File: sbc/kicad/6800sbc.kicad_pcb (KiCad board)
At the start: 2 copper layers, 104 parts, among them J1 AC/DC IN, J10 BAUD RATE, J11 SEGMENT TEST, J2 5V IN, J3 EXPANSION, J4 LTC, J5 Parallel Port, J6 TX DATA SELECT, J7 RX DATA SELECT, J8 USB POWER, J9 FTDI SERIAL, SW10 "9", SW11 "4", SW12 "5", SW13 "6", SW14 "1", SW15 "2", SW16 "3", SW17 "0", SW18 "RESET", SW2 "D", SW3 "E", SW4 "F", SW5 "A", SW6 "B", SW7 "C", SW8 "7", SW9 "8", U1 LM7805, U10 MAN71A, U11 MAN71A, U12 74LS259, U13 74LS259, U14 74LS259, U15 74LS259, U16 74LS259, U17 74LS259, U18 74LS244, U19 62256 RAM, U2 74LS00, U20 27128, U21 MC6802, U22 ATF16V8B, U23 74LS244, U24 74LS42, U3 74LS04, U4 6821, U5 MC6850, U6 MAN71A, U7 MAN71A, U8 MAN71A, U9 MAN71A, Y1 1.8432 MHz, Y2 3.579545 kHz

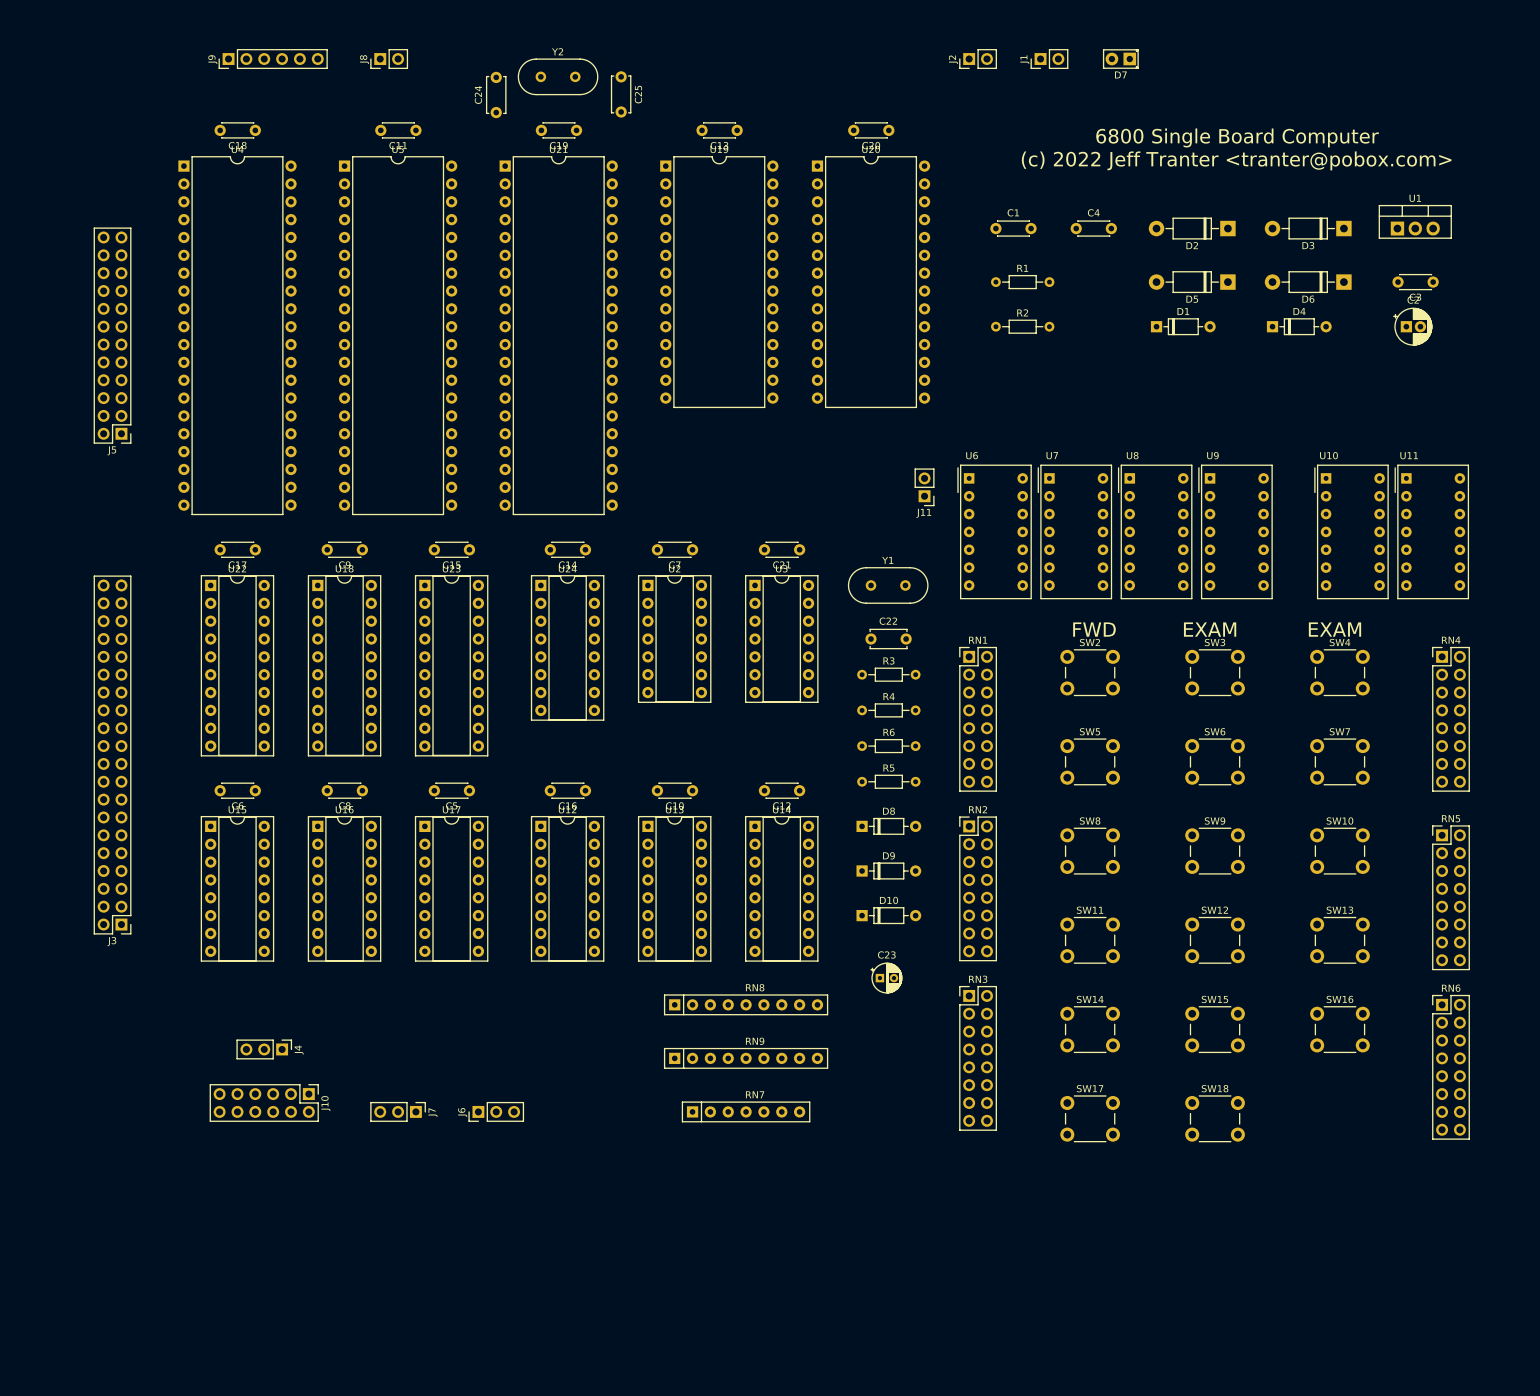
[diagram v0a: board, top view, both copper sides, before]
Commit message: Some fixes based on prototyping work.
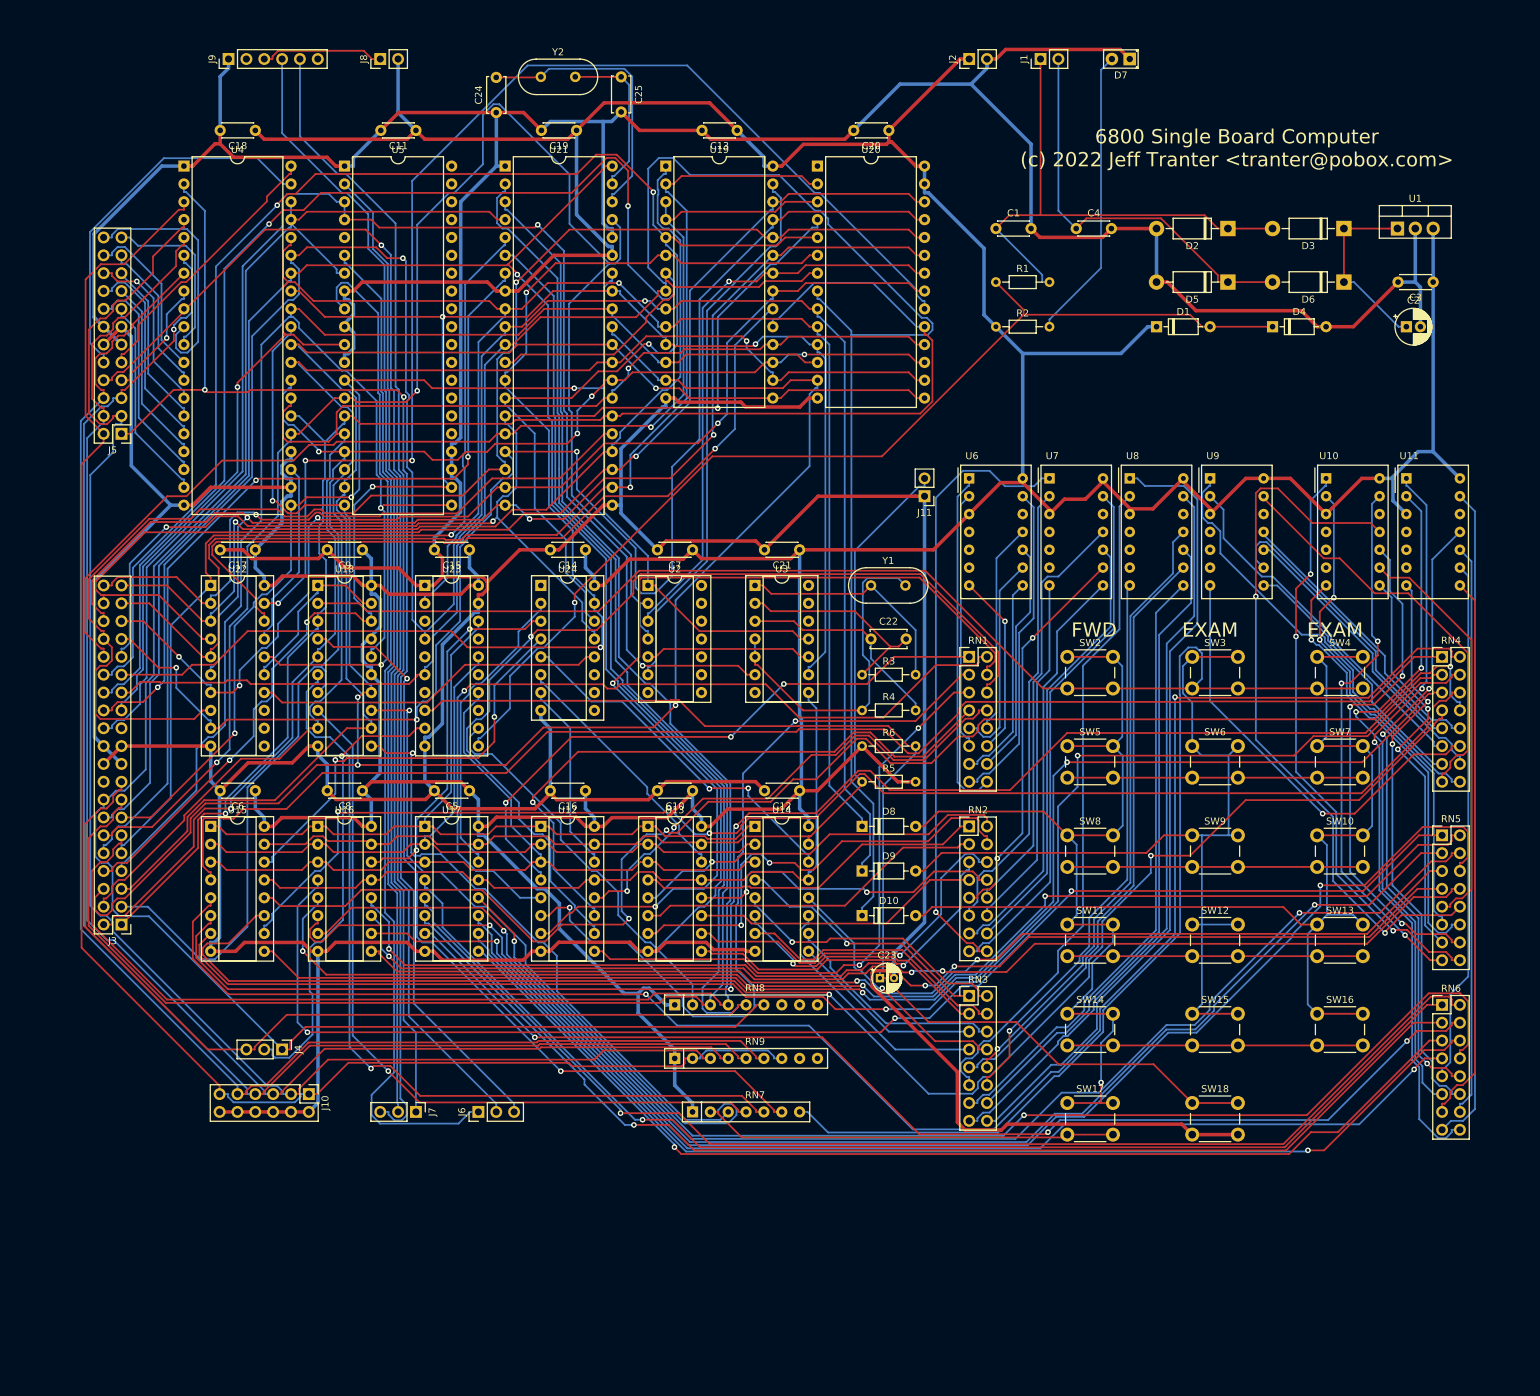
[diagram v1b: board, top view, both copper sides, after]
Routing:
- net GND: track 0.00 -> 998.2 mm
- net VCC: track 0.00 -> 904.0 mm
- net A1: track 0.00 -> 332.5 mm, vias 0 -> 3
- net ~RESET: track 0.00 -> 311.4 mm, vias 0 -> 1
- net A2: track 0.00 -> 298.9 mm
- net A0: track 0.00 -> 291.0 mm, vias 0 -> 2
- net Net-(RN7-Pad7): track 0.00 -> 276.5 mm
- net D2: track 0.00 -> 267.2 mm, vias 0 -> 4
- net ~IRQ: track 0.00 -> 262.0 mm
- net ~NMI: track 0.00 -> 256.9 mm
- net Net-(RN4-Pad2): track 0.00 -> 251.2 mm, vias 0 -> 2
- net D0: track 0.00 -> 249.0 mm, vias 0 -> 5
- net A5: track 0.00 -> 248.8 mm, vias 0 -> 3
- net ~HALT: track 0.00 -> 247.1 mm
- net MR: track 0.00 -> 239.9 mm
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
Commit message: Various updates.
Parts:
- removed RN1, RN2, RN3, RN4, RN5, RN6: 470, Connector_PinHeader_2.54mm:PinHeader_2x08_P2.54mm_Vertical
- added J12: REG. POWER, Connector_PinHeader_2.54mm:PinHeader_1x02_P2.54mm_Vertical, F.Cu at (199.4, 29.2)
- added R10: 470, Resistor_THT:R_Axial_DIN0204_L3.6mm_D1.6mm_P7.62mm_Horizontal, F.Cu at (168.9, 74.9)
- added R11: 470, Resistor_THT:R_Axial_DIN0204_L3.6mm_D1.6mm_P7.62mm_Horizontal, F.Cu at (168.9, 72.4)
- added R12: 470, Resistor_THT:R_Axial_DIN0204_L3.6mm_D1.6mm_P7.62mm_Horizontal, F.Cu at (168.9, 69.8)
- added R13: 470, Resistor_THT:R_Axial_DIN0204_L3.6mm_D1.6mm_P7.62mm_Horizontal, F.Cu at (168.9, 67.3)
- added R14: 470, Resistor_THT:R_Axial_DIN0204_L3.6mm_D1.6mm_P7.62mm_Horizontal, F.Cu at (168.9, 64.8)
- added R15: 470, Resistor_THT:R_Axial_DIN0204_L3.6mm_D1.6mm_P7.62mm_Horizontal, F.Cu at (180.3, 82.5)
- added R16: 470, Resistor_THT:R_Axial_DIN0204_L3.6mm_D1.6mm_P7.62mm_Horizontal, F.Cu at (180.3, 80.0)
- added R17: 470, Resistor_THT:R_Axial_DIN0204_L3.6mm_D1.6mm_P7.62mm_Horizontal, F.Cu at (180.3, 77.5)
- added R18: 470, Resistor_THT:R_Axial_DIN0204_L3.6mm_D1.6mm_P7.62mm_Horizontal, F.Cu at (180.3, 74.9)
- added R19: 470, Resistor_THT:R_Axial_DIN0204_L3.6mm_D1.6mm_P7.62mm_Horizontal, F.Cu at (180.3, 72.4)
- added R20: 470, Resistor_THT:R_Axial_DIN0204_L3.6mm_D1.6mm_P7.62mm_Horizontal, F.Cu at (180.3, 69.8)
- added R21: 470, Resistor_THT:R_Axial_DIN0204_L3.6mm_D1.6mm_P7.62mm_Horizontal, F.Cu at (180.3, 67.3)
- added R22: 470, Resistor_THT:R_Axial_DIN0204_L3.6mm_D1.6mm_P7.62mm_Horizontal, F.Cu at (180.3, 64.8)
- added R23: 470, Resistor_THT:R_Axial_DIN0204_L3.6mm_D1.6mm_P7.62mm_Horizontal, F.Cu at (191.8, 82.5)
- added R24: 470, Resistor_THT:R_Axial_DIN0204_L3.6mm_D1.6mm_P7.62mm_Horizontal, F.Cu at (191.8, 80.0)
- added R25: 470, Resistor_THT:R_Axial_DIN0204_L3.6mm_D1.6mm_P7.62mm_Horizontal, F.Cu at (191.8, 77.5)
- added R26: 470, Resistor_THT:R_Axial_DIN0204_L3.6mm_D1.6mm_P7.62mm_Horizontal, F.Cu at (191.8, 74.9)
- added R27: 470, Resistor_THT:R_Axial_DIN0204_L3.6mm_D1.6mm_P7.62mm_Horizontal, F.Cu at (191.8, 72.4)
- added R28: 470, Resistor_THT:R_Axial_DIN0204_L3.6mm_D1.6mm_P7.62mm_Horizontal, F.Cu at (191.8, 69.8)
- added R29: 470, Resistor_THT:R_Axial_DIN0204_L3.6mm_D1.6mm_P7.62mm_Horizontal, F.Cu at (191.8, 67.3)
- added R30: 470, Resistor_THT:R_Axial_DIN0204_L3.6mm_D1.6mm_P7.62mm_Horizontal, F.Cu at (191.8, 64.8)
- added R31: 470, Resistor_THT:R_Axial_DIN0204_L3.6mm_D1.6mm_P7.62mm_Horizontal, F.Cu at (203.2, 82.5)
- added R32: 470, Resistor_THT:R_Axial_DIN0204_L3.6mm_D1.6mm_P7.62mm_Horizontal, F.Cu at (203.2, 80.0)
- added R33: 470, Resistor_THT:R_Axial_DIN0204_L3.6mm_D1.6mm_P7.62mm_Horizontal, F.Cu at (203.2, 77.5)
- added R34: 470, Resistor_THT:R_Axial_DIN0204_L3.6mm_D1.6mm_P7.62mm_Horizontal, F.Cu at (203.2, 74.9)
- added R35: 470, Resistor_THT:R_Axial_DIN0204_L3.6mm_D1.6mm_P7.62mm_Horizontal, F.Cu at (203.2, 72.4)
- added R36: 470, Resistor_THT:R_Axial_DIN0204_L3.6mm_D1.6mm_P7.62mm_Horizontal, F.Cu at (203.2, 69.8)
- added R37: 470, Resistor_THT:R_Axial_DIN0204_L3.6mm_D1.6mm_P7.62mm_Horizontal, F.Cu at (203.2, 67.3)
- added R38: 470, Resistor_THT:R_Axial_DIN0204_L3.6mm_D1.6mm_P7.62mm_Horizontal, F.Cu at (203.2, 64.8)
- added R39: 470, Resistor_THT:R_Axial_DIN0204_L3.6mm_D1.6mm_P7.62mm_Horizontal, F.Cu at (219.7, 82.5)
- added R40: 470, Resistor_THT:R_Axial_DIN0204_L3.6mm_D1.6mm_P7.62mm_Horizontal, F.Cu at (219.7, 80.0)
- added R41: 470, Resistor_THT:R_Axial_DIN0204_L3.6mm_D1.6mm_P7.62mm_Horizontal, F.Cu at (219.7, 77.5)
- added R42: 470, Resistor_THT:R_Axial_DIN0204_L3.6mm_D1.6mm_P7.62mm_Horizontal, F.Cu at (219.7, 74.9)
- added R43: 470, Resistor_THT:R_Axial_DIN0204_L3.6mm_D1.6mm_P7.62mm_Horizontal, F.Cu at (219.7, 72.4)
- added R44: 470, Resistor_THT:R_Axial_DIN0204_L3.6mm_D1.6mm_P7.62mm_Horizontal, F.Cu at (219.7, 69.8)
- added R45: 470, Resistor_THT:R_Axial_DIN0204_L3.6mm_D1.6mm_P7.62mm_Horizontal, F.Cu at (219.7, 67.3)
- added R46: 470, Resistor_THT:R_Axial_DIN0204_L3.6mm_D1.6mm_P7.62mm_Horizontal, F.Cu at (219.7, 64.8)
- added R47: 470, Resistor_THT:R_Axial_DIN0204_L3.6mm_D1.6mm_P7.62mm_Horizontal, F.Cu at (231.1, 82.5)
- added R48: 470, Resistor_THT:R_Axial_DIN0204_L3.6mm_D1.6mm_P7.62mm_Horizontal, F.Cu at (231.1, 80.0)
- added R49: 470, Resistor_THT:R_Axial_DIN0204_L3.6mm_D1.6mm_P7.62mm_Horizontal, F.Cu at (231.1, 77.5)
- added R50: 470, Resistor_THT:R_Axial_DIN0204_L3.6mm_D1.6mm_P7.62mm_Horizontal, F.Cu at (231.1, 74.9)
- added R51: 470, Resistor_THT:R_Axial_DIN0204_L3.6mm_D1.6mm_P7.62mm_Horizontal, F.Cu at (231.1, 72.4)
- added R52: 470, Resistor_THT:R_Axial_DIN0204_L3.6mm_D1.6mm_P7.62mm_Horizontal, F.Cu at (231.1, 69.8)
- added R53: 470, Resistor_THT:R_Axial_DIN0204_L3.6mm_D1.6mm_P7.62mm_Horizontal, F.Cu at (231.1, 67.3)
- added R54: 470, Resistor_THT:R_Axial_DIN0204_L3.6mm_D1.6mm_P7.62mm_Horizontal, F.Cu at (231.1, 64.8)
- added R7: 470, Resistor_THT:R_Axial_DIN0204_L3.6mm_D1.6mm_P7.62mm_Horizontal, F.Cu at (168.9, 82.5)
- added R8: 470, Resistor_THT:R_Axial_DIN0204_L3.6mm_D1.6mm_P7.62mm_Horizontal, F.Cu at (168.9, 80.0)
- added R9: 470, Resistor_THT:R_Axial_DIN0204_L3.6mm_D1.6mm_P7.62mm_Horizontal, F.Cu at (168.9, 77.5)
- moved C1 14.0 mm to (172.7, 39.4)
- moved C4 14.0 mm to (184.2, 39.4)
- moved D2 14.0 mm to (205.7, 39.4)
- moved D3 14.0 mm to (222.2, 39.4)
- moved U1 14.0 mm to (229.9, 39.4)
- moved C2 14.0 mm to (231.1, 53.3)
- moved C3 14.0 mm to (234.9, 47.0)
- moved D1 14.0 mm to (195.6, 53.3)
- moved D4 14.0 mm to (212.1, 53.3)
- moved D5 14.0 mm to (205.7, 47.0)
- moved D6 14.0 mm to (222.2, 47.0)
- moved R1 14.0 mm to (172.7, 47.0)
- moved R2 14.0 mm to (172.7, 53.3)
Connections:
- C3 pad 1: VCC -> Net-(C3-Pad1)
- J10 pad 11: PA1 -> PA6
- RN9 pad 7: PA1 -> PA6
- U1 pad 3: VCC -> Net-(C3-Pad1)
- U19 pad 4: A7 -> A6
- U2 pad 10: (no net) -> GND
- U2 pad 12: (no net) -> GND
- U2 pad 13: (no net) -> GND
- U2 pad 9: (no net) -> GND
- U20 pad 1: (no net) -> VCC
- U3 pad 13: (no net) -> GND
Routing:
- net VCC: track 904.0 -> 896.4 mm
- net Net-(C3-Pad1): track 0.00 -> 7.62 mm
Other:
- board text added: "AUTO"
- board text added: "BACK"
- board text added: "CHAN"
- board text added: "DO"

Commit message: Getting close to ready to order PCBs. Check in all files.
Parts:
- removed RN7: 8K2, Resistor_THT:R_Array_SIP7
- removed RN8, RN9: 3K, Resistor_THT:R_Array_SIP9
- added H1: MountingHole_3mm, MountingHole:MountingHole_3mm, F.Cu at (39.4, 29.2)
- added H2: MountingHole_3mm, MountingHole:MountingHole_3mm, F.Cu at (215.9, 27.9)
- added H3: MountingHole_3mm, MountingHole:MountingHole_3mm, F.Cu at (38.1, 210.8)
- added H4: MountingHole_3mm, MountingHole:MountingHole_3mm, F.Cu at (215.9, 210.8)
- added J13: PA2, Connector_PinHeader_2.54mm:PinHeader_1x03_P2.54mm_Vertical, F.Cu at (74.9, 188.0)
- added J14: PA3, Connector_PinHeader_2.54mm:PinHeader_1x03_P2.54mm_Vertical, F.Cu at (78.7, 188.0)
- added J15: PA4, Connector_PinHeader_2.54mm:PinHeader_1x03_P2.54mm_Vertical, F.Cu at (82.5, 188.0)
- added J16: PA5, Connector_PinHeader_2.54mm:PinHeader_1x03_P2.54mm_Vertical, F.Cu at (86.4, 188.0)
- added J17: PA6, Connector_PinHeader_2.54mm:PinHeader_1x03_P2.54mm_Vertical, F.Cu at (90.2, 188.0)
- added R55: 8K2, Resistor_THT:R_Axial_DIN0204_L3.6mm_D1.6mm_P7.62mm_Horizontal, F.Cu at (128.3, 179.1)
- added R56: 8K2, Resistor_THT:R_Axial_DIN0204_L3.6mm_D1.6mm_P7.62mm_Horizontal, F.Cu at (128.3, 172.7)
- added R57: 8K2, Resistor_THT:R_Axial_DIN0204_L3.6mm_D1.6mm_P7.62mm_Horizontal, F.Cu at (128.3, 167.6)
- added R58: 8K2, Resistor_THT:R_Axial_DIN0204_L3.6mm_D1.6mm_P7.62mm_Horizontal, F.Cu at (128.3, 162.6)
- added R59: 8K2, Resistor_THT:R_Axial_DIN0204_L3.6mm_D1.6mm_P7.62mm_Horizontal, F.Cu at (128.3, 157.5)
- added R60: 8K2, Resistor_THT:R_Axial_DIN0204_L3.6mm_D1.6mm_P7.62mm_Horizontal, F.Cu at (128.3, 152.4)
- added R61: 3K, Resistor_THT:R_Axial_DIN0204_L3.6mm_D1.6mm_P7.62mm_Horizontal, F.Cu at (128.3, 210.8)
- added R62: 3K, Resistor_THT:R_Axial_DIN0204_L3.6mm_D1.6mm_P7.62mm_Horizontal, F.Cu at (128.3, 204.5)
- added R63: 3K, Resistor_THT:R_Axial_DIN0204_L3.6mm_D1.6mm_P7.62mm_Horizontal, F.Cu at (128.3, 198.1)
- added R64: 3K, Resistor_THT:R_Axial_DIN0204_L3.6mm_D1.6mm_P7.62mm_Horizontal, F.Cu at (128.3, 191.8)
- added R65: 3K, Resistor_THT:R_Axial_DIN0204_L3.6mm_D1.6mm_P7.62mm_Horizontal, F.Cu at (128.3, 185.4)
- J10: value BAUD RATE -> PA1; footprint Connector_PinHeader_2.54mm:PinHeader_2x06_P2.54mm_Vertical -> Connector_PinHeader_2.54mm:PinHeader_1x03_P2.54mm_Vertical
- J5: value Parallel Port -> PARALLEL PORT
- U19: value 62256 RAM -> 62256
- U5: footprint Package_DIP:DIP-40_W15.24mm -> Package_DIP:DIP-24_W15.24mm
- Y2: value 3.579545 kHz -> 3.579545 MHz
- moved J7 147.1 mm to (48.3, 38.1), turned to 90 degrees
- moved J6 146.0 mm to (61.0, 38.1)
- moved J4 140.3 mm to (83.8, 30.5), turned to 90 degrees
- moved U15 140.3 mm to (175.3, 57.1)
- moved U16 139.2 mm to (189.2, 57.1)
- moved U17 138.2 mm to (203.2, 57.1)
- moved C6 108.8 mm to (139.7, 52.1)
- moved C8 108.0 mm to (153.7, 52.1)
- moved C5 107.2 mm to (167.6, 52.1)
- moved C16 105.5 mm to (181.6, 52.1)
- moved C10 104.7 mm to (195.6, 52.1)
- moved C12 103.9 mm to (209.6, 52.1)
- moved U12 85.2 mm to (133.3, 57.1)
- moved U13 84.8 mm to (147.3, 57.1)
- moved U14 84.4 mm to (161.3, 57.1)
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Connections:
- J10 pad 1: PA1 -> VCC
- J10 pad 2: GND -> PA1
- J10 pad 3: PA2 -> GND
- U2 pad 14: (no net) -> VCC
- U2 pad 7: (no net) -> GND
- U3 pad 14: (no net) -> VCC
- U3 pad 7: (no net) -> GND
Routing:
- net Net-(R32-Pad2): track 251.2 -> 41.5 mm, vias 2 -> 0
- net Net-(R37-Pad2): track 225.1 -> 17.2 mm, vias 2 -> 0
- net Net-(R38-Pad2): track 206.7 -> 15.5 mm, vias 3 -> 0
- net Net-(R34-Pad2): track 216.9 -> 27.5 mm, vias 2 -> 0
- net Net-(R33-Pad2): track 220.2 -> 34.7 mm, vias 2 -> 0
- net Net-(R35-Pad2): track 199.2 -> 18.6 mm, vias 2 -> 0
- net Net-(R44-Pad2): track 196.9 -> 18.3 mm, vias 2 -> 0
- net Net-(R36-Pad2): track 196.2 -> 17.9 mm, vias 3 -> 0
- net Net-(R42-Pad2): track 197.2 -> 27.4 mm, vias 2 -> 0
- net Net-(R41-Pad2): track 197.6 -> 34.7 mm, vias 2 -> 0
- net Net-(R54-Pad2): track 174.6 -> 15.1 mm, vias 2 -> 0
- net ~DISP5EN: track 52.3 -> 211.5 mm, vias 2 -> 1
- net ~DISP6EN: track 43.3 -> 198.0 mm
- net Net-(J6-Pad2): track 162.8 -> 9.20 mm
- net Net-(R46-Pad2): track 169.0 -> 15.5 mm, vias 3 -> 0
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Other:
- board outline added: 188 x 193 mm
- board text added: "+"
- board text added: "-"
- board text added: "0"
- board text added: "1"
- board text added: "2"
- board text added: "3"
- board text added: "4"
- board text added: "5"
- board text added: "6"
- board text added: "7"
- board text added: "8"
- board text added: "9"
- board text added: "A"
- board text added: "A0"
- board text added: "A1"
- board text added: "A10"
- board text added: "A11"
- board text added: "A12"
- board text added: "A13"
- board text added: "A14"
- board text added: "A15"
- board text added: "A2"
- board text added: "A3"
- board text added: "A4"
- board text added: "A5"
- board text added: "A6"
- board text added: "A7"
- board text added: "A8"
- board text added: "A9"
- board text added: "ACCA"
- board text added: "ACCB"
- board text added: "B"
- board text added: "BA"
- board text added: "BR"
- board text added: "C"
- board text added: "CA1"
- board text added: "CA2"
- board text added: "CB1"
- board text added: "CB2"
- board text added: "CC"
- board text added: "D"
- board text added: "D0"
- board text added: "D1"
- board text added: "D2"
- board text added: "D3"
- board text added: "D4"
- board text added: "D5"
- board text added: "D6"
- board text added: "D7"
- board text added: "E"
- board text added: "F"
- board text added: "GND"
- board text added: "H"
- board text added: "I"
- board text added: "INDEX"
- board text added: "MR"
- board text added: "N"
- board text added: "PA0"
- board text added: "PA1"
- board text added: "PA2"
- board text added: "PA3"
- board text added: "PA4"
- board text added: "PA5"
- board text added: "PA6"
- board text added: "PA7"
- board text added: "PB0"
- board text added: "PB1"
- board text added: "PB2"
- board text added: "PB3"
- board text added: "PB4"
- board text added: "PB5"
- board text added: "PB6"
- board text added: "PB7"
- board text added: "PC"
- board text added: "RESET"
- board text added: "RTI"
- board text added: "R~W"
- board text added: "SCLK"
- board text added: "SP"
- board text added: "SS"
- board text added: "V"
- board text added: "VCC"
- board text added: "VMA"
- board text added: "Z"
- board text added: "~HALT"
- board text added: "~IRQ"
- board text added: "~NMI"
- board text added: "~RESET"

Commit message: Optimizing board layout.
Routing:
- net ~IRQ: track 287.5 -> 351.5 mm, vias 2 -> 0
- net ~NMI: track 238.0 -> 300.3 mm, vias 2 -> 0
- net A0: track 268.5 -> 321.2 mm, vias 6 -> 0
- net A1: track 230.7 -> 274.8 mm, vias 1 -> 0
- net MR: track 194.3 -> 235.9 mm, vias 0 -> 1
- net D5: track 299.0 -> 258.7 mm, vias 2 -> 1
- net ~RESET: track 277.7 -> 238.7 mm, vias 2 -> 1
- net GND: track 994.3 -> 1027.5 mm
- net A7: track 234.2 -> 202.4 mm, vias 2 -> 1
- net 60HZ: track 163.1 -> 192.4 mm, vias 0 -> 1
- net VCC: track 931.5 -> 960.4 mm
- net VMA: track 198.2 -> 173.1 mm
- net R~W: track 239.0 -> 214.1 mm, vias 4 -> 2
- net PA3: track 148.7 -> 170.1 mm
- net ~READ: track 146.6 -> 125.4 mm, vias 2 -> 1
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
